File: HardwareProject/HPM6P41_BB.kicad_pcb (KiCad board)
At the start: 4 copper layers, 152.8 x 80.3 mm, 293 parts, among them J1 USB_B, J10 Conn_01x01, J11 Conn_01x01, J12 Conn_01x01, J2 USB_C_Receptacle_USB2.0_16P, J3 Conn_02x16_Odd_Even, J4 Conn_ARM_JTAG_SWD_20, J5 Conn_01x03, J6 Conn_01x03, J7 SMA, J8 SMA, J9 Conn_01x01, Q1 HYG080N10LS1C2, Q2 HYG080N10LS1C2, Q3 HYG080N10LS1C2, Q4 HYG080N10LS1C2, Q5 S8050, Q7 S8050, SW1 焊盘, SW2 Push_Button, SW3 Push_Button, SW4 Push_Button, U1 UCC27211ADRMR, U10 TJA1044GTK/3Z, U11 TPS54302, U12 LP5907MFX-3.3, U13 REF3030, U14 LM5164DDA, U15 SY8089, U16 INA241A3xDDF, U17 INA241A3xDDF, U18 UCC27519, U19 XC6206PxxxMR, U2 UCC27211ADRMR, U20 SGM8551XN, U21 SGM8551XN, U22 TMP112xxDRL, U23 TPD4E05U06DQA, U3 UCC27519, U4 HPM6P41IPB1, U5 TPD4E05U06DQA, U6 AT24C08C-SSHM-T, U7 TMP112xxDRL, U8 TMP112xxDRL, U9 SIT3088ETK, Y1 24MHz ±10ppm 6pF

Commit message: 修改了UCC27211A封装，此芯片此前的封装均错误 修改了采样线布局，为SAR ADC加入前置RC
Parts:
- added C93: 47pF,50V, Capacitor_SMD:C_0603_1608Metric, F.Cu at (147.2, 96.8)
- added C94: 47pF,50V, Capacitor_SMD:C_0603_1608Metric, F.Cu at (151.7, 96.8)
- added C95: 47pF,50V, Capacitor_SMD:C_0603_1608Metric, F.Cu at (150.2, 96.8)
- added C96: 47pF,50V, Capacitor_SMD:C_0603_1608Metric, F.Cu at (148.7, 96.8)
- added C97: 100nF,10V, Capacitor_SMD:C_0603_1608Metric, F.Cu at (122.8, 72.2)
- added C98: 100nF,10V, Capacitor_SMD:C_0603_1608Metric, F.Cu at (182.8, 74.7)
- added C99: 22uF,10V, Capacitor_SMD:C_0603_1608Metric, B.Cu at (134.9, 83.0)
- added R73: 33Ω, Resistor_SMD:R_0603_1608Metric, F.Cu at (144.9, 96.0)
- added R74: 33Ω, Resistor_SMD:R_0603_1608Metric, F.Cu at (153.9, 96.0)
- added R75: 33Ω, Resistor_SMD:R_0603_1608Metric, F.Cu at (153.9, 97.5)
- added R76: 33Ω, Resistor_SMD:R_0603_1608Metric, F.Cu at (144.9, 97.5)
- U1, U2: footprint HPM6P41_BB:VSON-8-1EP_3x3mm_P0.65mm_EP1.65x2.4mm -> TexasInstruments:DRM8_3P38X2P45_TEX
- moved FB5 6.82 mm to (130.2, 82.4), turned to 0 degrees
- moved C65 5.60 mm to (132.8, 87.3), turned to -90 degrees
- moved C62 3.84 mm to (130.2, 83.9), turned to 180 degrees
- moved D19 3.55 mm to (182.2, 68.0), turned to -90 degrees
- moved D16 3.44 mm to (118.4, 68.0)
- moved R32 3.30 mm to (152.3, 100.2), turned to 180 degrees
- moved U12 1.88 mm to (130.2, 86.7), turned to -90 degrees
- moved U5 1.77 mm to (148.6, 100.2)
- moved D2 1.59 mm to (121.5, 60.7)
- moved R4 1.59 mm to (121.6, 59.0)
- moved R5 1.59 mm to (121.6, 57.5)
- moved R9 1.59 mm to (121.5, 62.4)
- moved FB4 1.40 mm to (133.6, 84.3), turned to 90 degrees
- moved D4 1.32 mm to (179.5, 60.3)
- moved R13 1.32 mm to (179.4, 62.0)
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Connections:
- C62 pad 1: Net-(U12-EN) -> Net-(U12-IN)
- FB5 pad 2: Net-(U12-EN) -> Net-(U12-IN)
- R57 pad 2: /PD6 -> Net-(R57-Pad2)
- R58 pad 2: /PD9 -> Net-(R58-Pad2)
- U12 pad 1: Net-(U12-EN) -> Net-(U12-IN)
- U12 pad 3: Net-(U12-EN) -> +5V
- U16 pad 5: /PD7 -> Net-(R73-Pad1)
- U17 pad 5: /PD8 -> Net-(R74-Pad1)
- U20 pad 1: /PD6 -> Net-(R57-Pad2)
- U21 pad 1: /PD9 -> Net-(R58-Pad2)
- U5 pad 4: VBUS -> +5V
- U5 pad 5: VBUS -> +5V
- U5 pad 6: VBUS -> +5V
- U5 pad 7: VBUS -> +5V
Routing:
- net /PD9: track 72.6 -> 7.85 mm, vias 2 -> 0
- net /PD6: track 68.4 -> 9.00 mm
- net Net-(R58-Pad2): track 0.00 -> 57.3 mm
- net Net-(R57-Pad2): track 0.00 -> 55.3 mm
- net /PD8: track 64.6 -> 10.0 mm, vias 2 -> 0
- net Net-(R74-Pad1): track 0.00 -> 51.6 mm
- net /PD7: track 57.1 -> 10.5 mm
- net Net-(R73-Pad1): track 0.00 -> 44.9 mm
- net GND: track 604.5 -> 647.9 mm, vias 230 -> 238
- net VANA: track 166.4 -> 146.5 mm, vias 10 -> 8
- net +5V: track 182.5 -> 196.8 mm, vias 7 -> 12
- net VBUS: track 59.5 -> 46.0 mm
- net Net-(U12-EN): track 8.27 -> 0.00 mm
- net USB_DP: track 46.6 -> 54.5 mm, vias 0 -> 2
- net USB_DN: track 45.1 -> 52.9 mm, vias 0 -> 2
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- removed copper zone on F.Cu, net VANA
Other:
- board text added: "2025-6-13 Alipay Rev3"
- board text removed: "2025-5-22 Alipay Rev2"

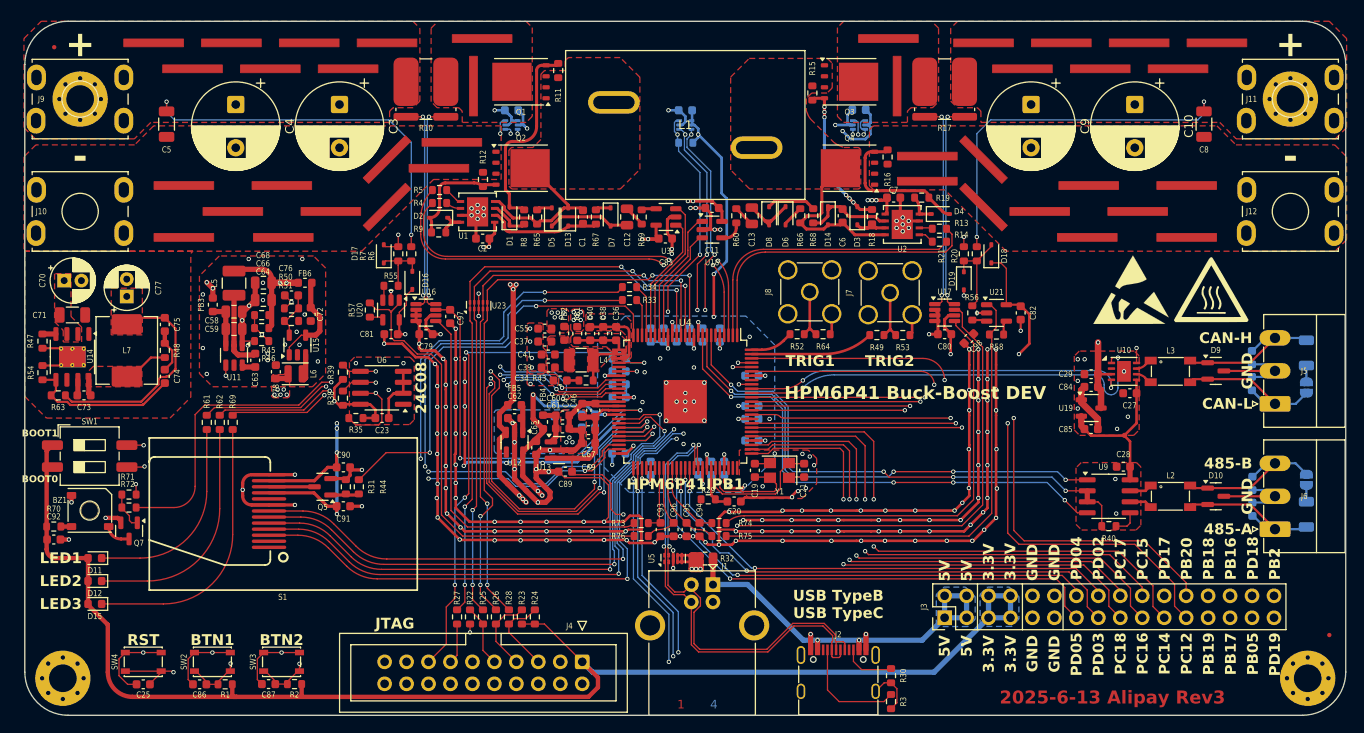
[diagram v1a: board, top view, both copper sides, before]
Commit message: 换掉UCC27519，它居然要55%VDD才到逻辑高，换成UCC2751
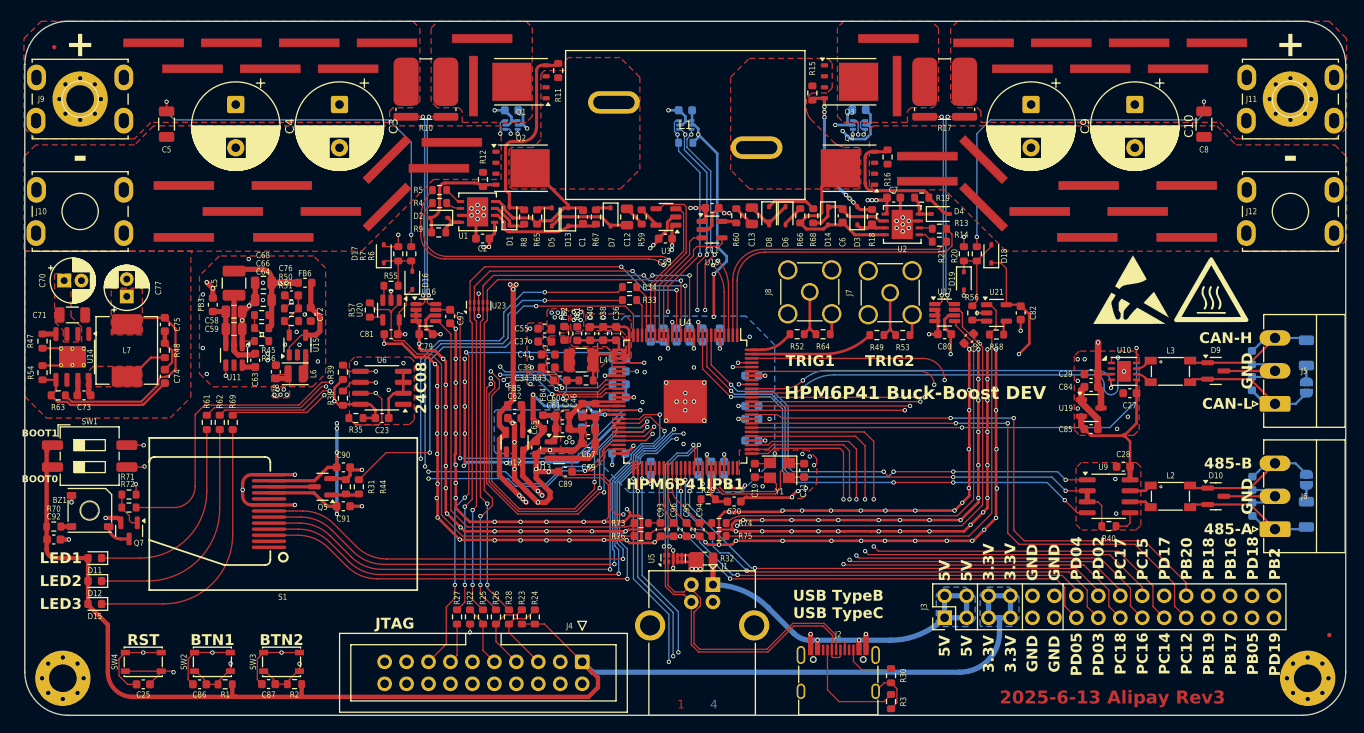
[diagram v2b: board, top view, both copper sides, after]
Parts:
- R48: value 309k -> 357k
- R54: value 101k -> 50k
- R63: value 665k -> 453k
- U18, U3: value UCC27519 -> UCC27517
- turned C11 to 0 degrees
- turned C83 to 180 degrees
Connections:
- R59 pad 2: Net-(U3-OUT) -> Net-(U3-V_{DD})
- U18 pad 1: /PA18 -> Vdrv
- U18 pad 3: /PA19 -> /PA18
- U18 pad 4: Net-(U18-OUT) -> /PA19
- U18 pad 5: Vdrv -> Net-(U18-OUT)
- U3 pad 1: /PA16 -> Vdrv
- U3 pad 3: /PA17 -> /PA16
- U3 pad 4: Net-(U3-OUT) -> /PA17
- U3 pad 5: Vdrv -> Net-(U3-V_{DD})
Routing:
- net GND: track 647.9 -> 681.1 mm, vias 238 -> 236
- net +5V: track 196.8 -> 207.7 mm
- net VANA: track 146.5 -> 151.5 mm
- net Vdrv: track 57.6 -> 53.3 mm
- net /PA17: track 16.8 -> 20.2 mm
- net +3.3V: track 370.8 -> 373.7 mm
- net Net-(U3-V_{DD}): track 0.00 -> 2.46 mm
- net /PA16: track 14.8 -> 17.2 mm
- net /PA19: track 13.3 -> 15.6 mm
- net Net-(U3-OUT): track 1.71 -> 0.00 mm
- net /PA18: track 15.5 -> 13.9 mm
- net Net-(U18-OUT): track 2.85 -> 1.73 mm
- net VBUS: track 46.0 -> 45.0 mm
